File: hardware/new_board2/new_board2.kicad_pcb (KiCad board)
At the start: 2 copper layers, 80 x 110 mm, 55 parts, among them CON1 BARREL_JACK, J1 Conn_01x02, J10 Conn_01x02, J11 Conn_01x02, J12 Conn_01x02, J13 Conn_01x02, J14 Conn_01x02, J2 Conn_01x02, J3 Conn_01x02, J4 Conn_01x02, J5 Conn_01x02, J6 Conn_01x02, J7 Conn_01x02, J8 Conn_01x02, J9 Conn_01x02, P1 Conn_01x02, P10 D4, P11 D6, P12 D8, P13 A2, P14 A3, P15 I2C 1, P16 I2C 2, P17 Conn_01x02, P18 Conn_01x02, P2 Conn_01x02, P3 Conn_01x02, P5 Conn_01x02, P6 D7, P7 A1, P8 UART, U1 LM2596T-5, U2 ESP32-DEVKITC-32D

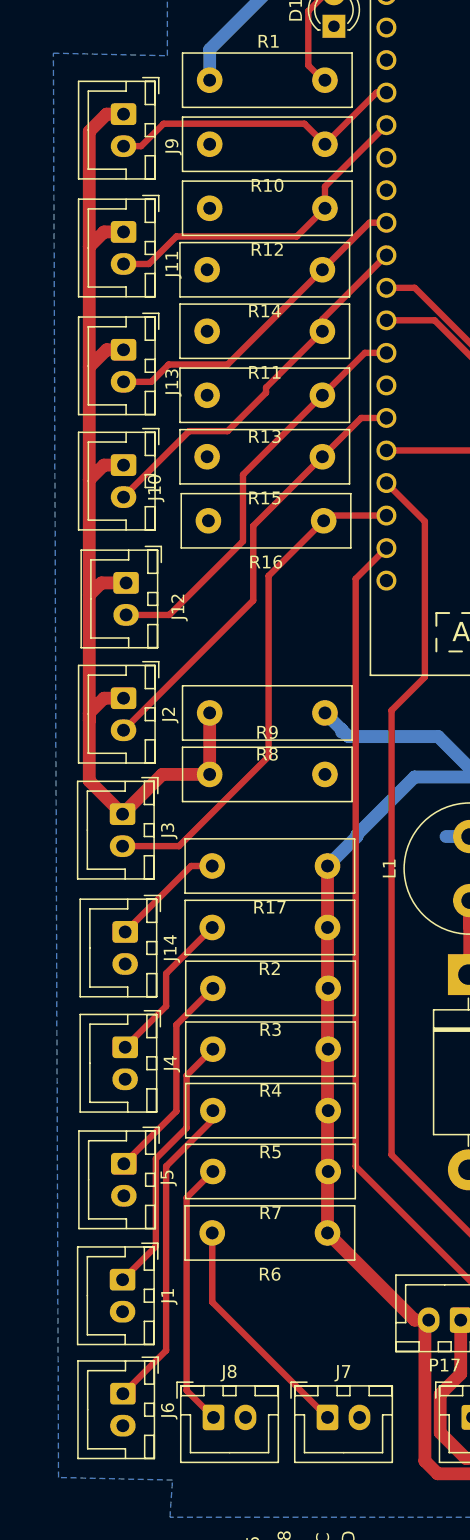
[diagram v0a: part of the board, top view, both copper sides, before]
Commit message: add first version of new board
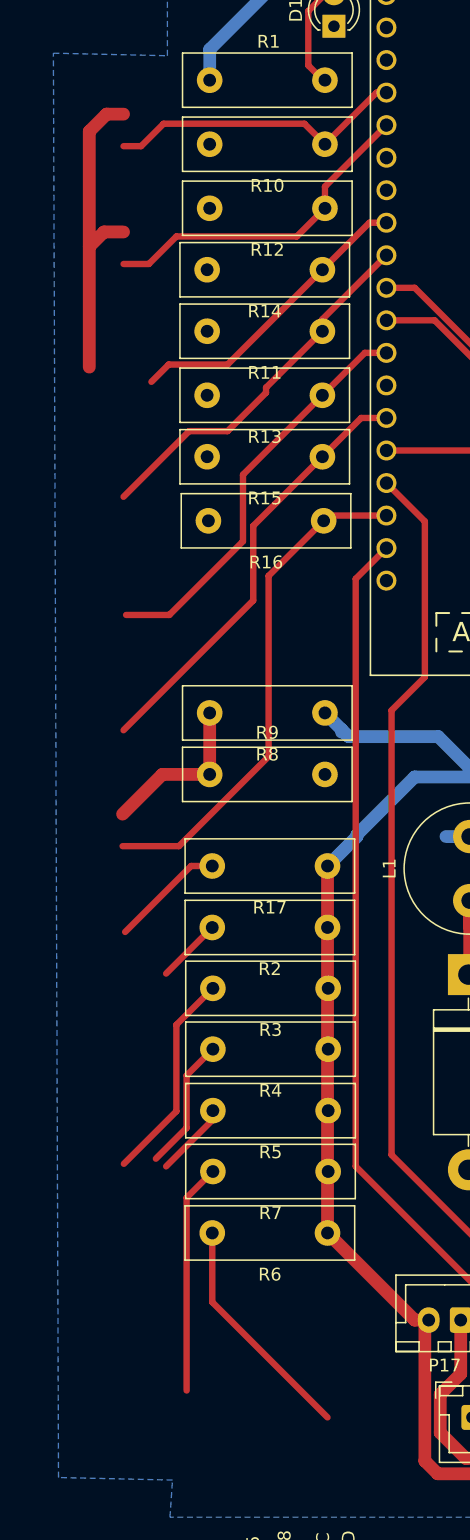
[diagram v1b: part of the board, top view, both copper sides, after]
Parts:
- removed J1, J10, J11, J12, J13, J14, J2, J3, J4, J5, J6, J7, J8, J9: Conn_01x02, Connector_JST:JST_XH_B2B-XH-A_1x02_P2.50mm_Vertical
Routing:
- net +3V3: track 87.1 -> 37.7 mm
- net Net-(J6-Pin_1): track 25.0 -> 5.86 mm
- net Net-(J1-Pin_1): track 20.9 -> 10.4 mm
- net Net-(J4-Pin_1): track 12.2 -> 5.09 mm
- net Net-(J8-Pin_1): track 20.9 -> 17.9 mm
- net D3-3: track 25.8 -> 23.7 mm
